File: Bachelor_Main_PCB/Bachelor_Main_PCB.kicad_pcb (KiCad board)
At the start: 4 copper layers, 200 x 81.5 mm, 220 parts, among them IC1 LD3985M18R, J1 M20-9990245, J11 F32Q-1A7H1-11022, J13 CONMHF1-SMD-G-T, J14 CONMHF1-SMD-G-T, J2 M20-9990245, J21 CONMHF1-SMD-G-T, J25 M20-9990245, J26 691137710002, J27 Conn_01x03_Pin, J28 691137710002, J29 M20-9990245, J4 MEM2075-00-140-01-A, J8 Conn_01x07_Pin, J9 M20-9990245, P1 SF70S006VBAR2000, Q1 SSM3J358R,LF, Q10 NX3008NBKW, Q11 SSM3J358R,LF, Q12 NX3008NBKW, Q13 BC817-40Q-13-F, Q2 SSM3J358R,LF, Q3 NX3008NBKW, Q4 NX3008NBKW, Q5 NX3008NBKW, Q6 NX3008NBKW, Q7 NX3008NBKW, Q8 NX3008NBKW, Q9 NX3008NBKW, U1 USB3320C-EZK-TR, U10 LMR51450FNDRRR, U11 USB2514B-I/M2, U2 STM32H7A3ZITxQ, U3 ESD7004MUTAG, U4 ESD7004MUTAG, U5 SC0683, U6 ESD7004MUTAG, U7 RC7620_1104627, U8 LM73100RPWR, U9 LMR51450FNDRRR, Y1 ECS-327TXO-30-TR, Y2 SG-210STF 24Mhz

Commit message: add gnd plane and fixed MCU bypass cap trace error
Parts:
- moved R18 93.2 mm to (153.2, 66.3), turned to 180 degrees
- moved R17 89.0 mm to (152.4, 68.8), turned to 90 degrees
- moved R16 85.8 mm to (148.3, 69.5)
- moved D4 85.3 mm to (152.4, 77.7), turned to 180 degrees
- moved Q2 84.0 mm to (148.4, 72.9), turned to -90 degrees
- moved J9 84.0 mm to (144.9, 68.7), turned to -90 degrees
- moved Q3 81.0 mm to (151.6, 72.7), turned to -90 degrees
- moved R19 80.4 mm to (149.2, 77.7)
- moved J11 77.8 mm to (94.6, 50.8), turned to 0 degrees
- moved J8 30.1 mm to (68.8, 105.3)
- moved Q6 1.46 mm to (209.9, 79.0)
- moved R29 1.46 mm to (209.7, 81.5)
- moved R30 1.46 mm to (209.7, 76.2)
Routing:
- net GND: track 54.3 -> 47.7 mm
- net +3V5_MCU: track 53.9 -> 48.8 mm
- added copper zone on In1.Cu, net GND

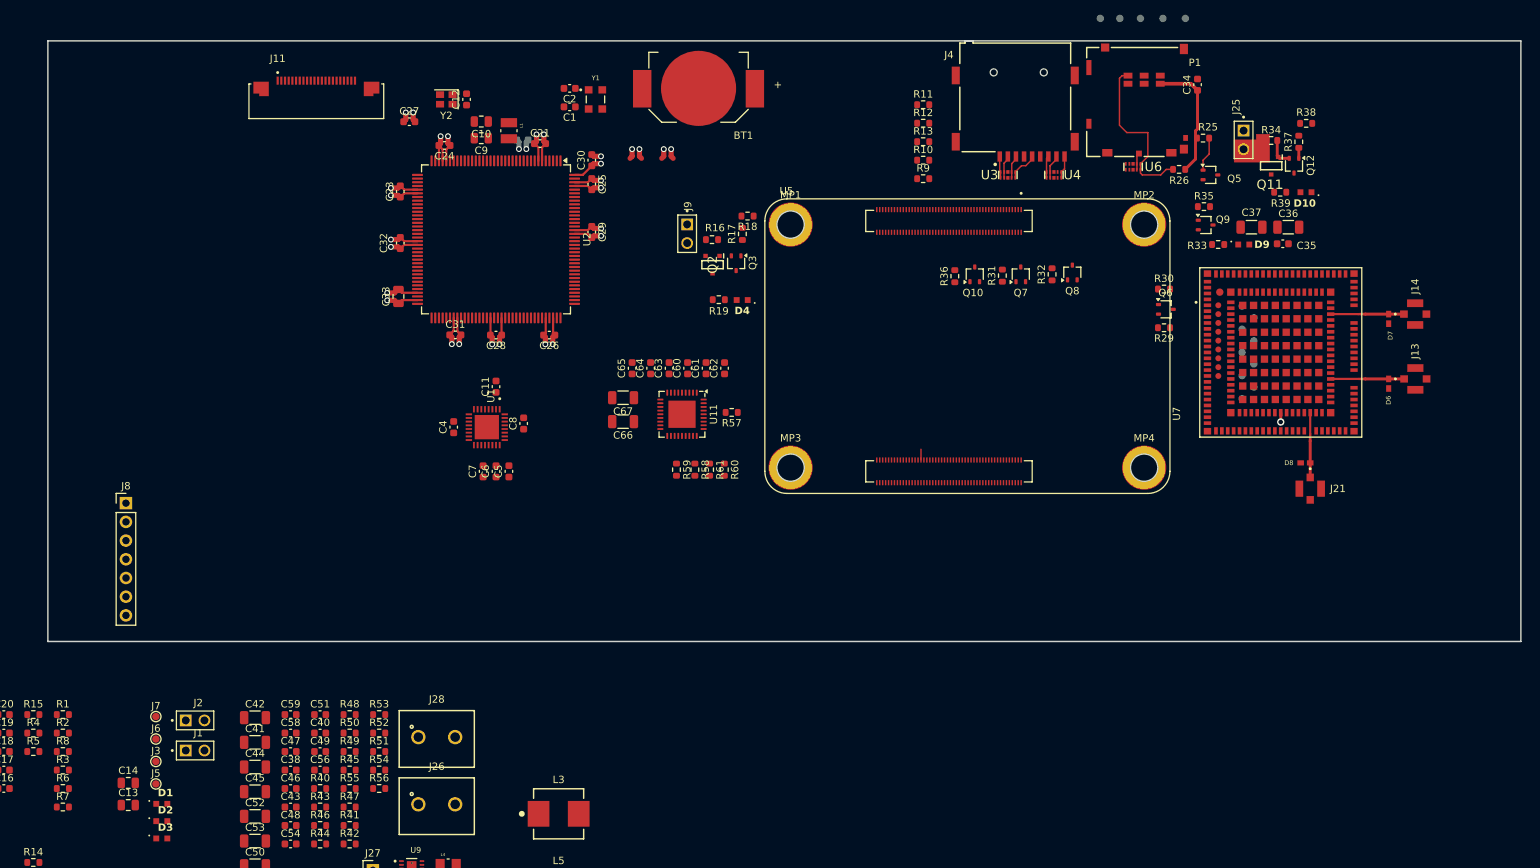
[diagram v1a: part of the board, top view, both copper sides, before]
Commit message: Updated gnd planes
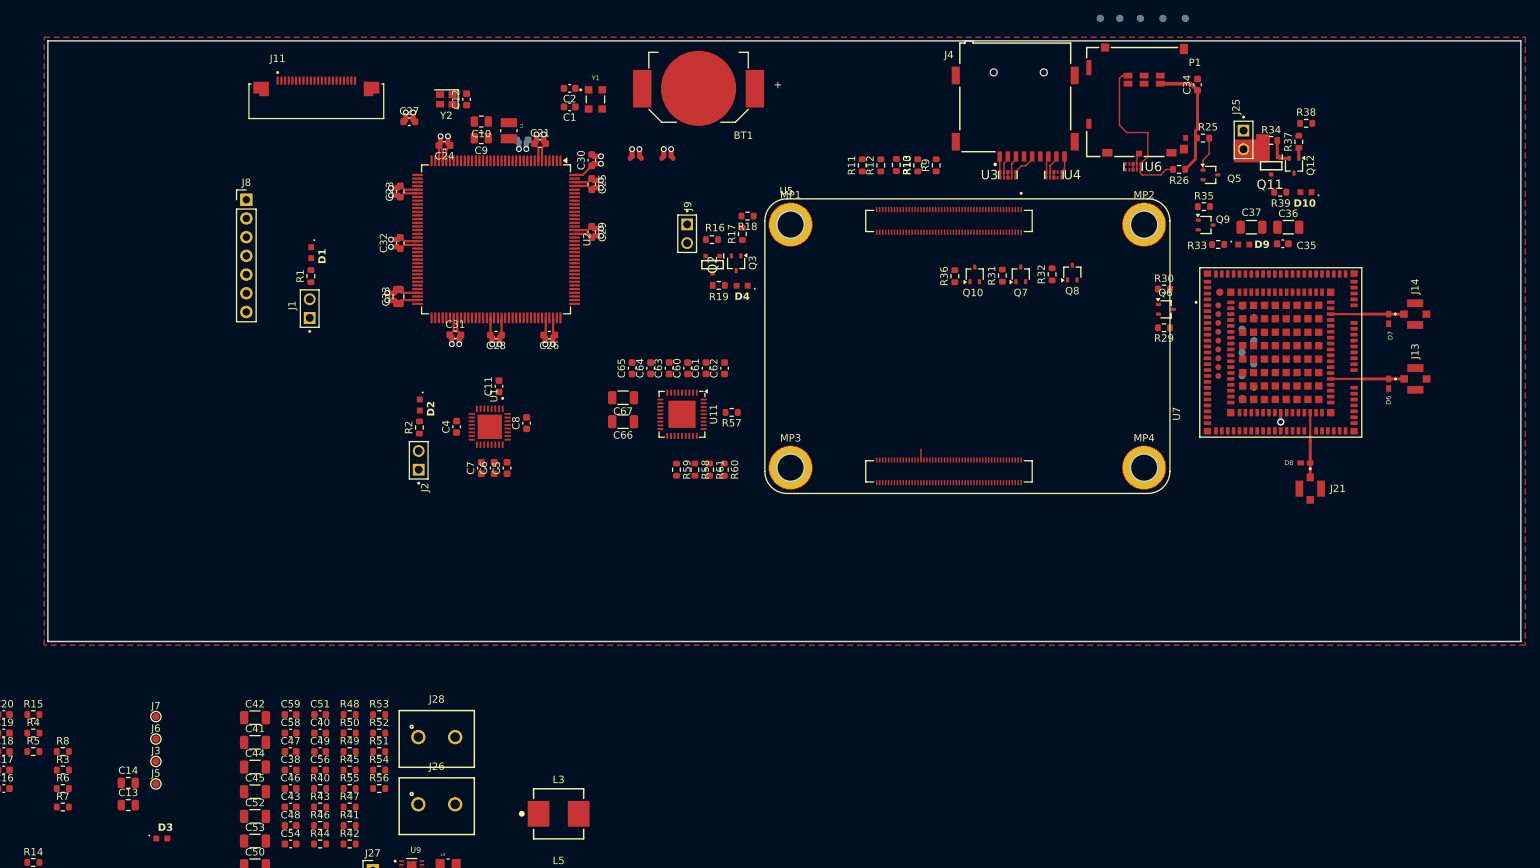
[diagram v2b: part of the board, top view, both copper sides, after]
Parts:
- moved D1 77.5 mm to (93.9, 71.3), turned to -90 degrees
- moved R1 68.4 mm to (93.9, 74.5), turned to 90 degrees
- moved D2 66.5 mm to (108.7, 92.0), turned to -90 degrees
- moved R2 63.8 mm to (108.6, 95.0), turned to 90 degrees
- moved J1 62.0 mm to (93.7, 78.9), turned to 90 degrees
- moved J2 46.6 mm to (108.5, 99.5), turned to 90 degrees
- moved J8 44.3 mm to (85.1, 64.1)
- moved R11 11.7 mm to (168.7, 59.5), turned to 90 degrees
- moved R12 8.12 mm to (171.2, 59.5), turned to 90 degrees
- moved R13 4.83 mm to (173.3, 59.4), turned to -90 degrees
- moved R9 2.53 mm to (178.8, 59.5), turned to 90 degrees
- moved D4 1.94 mm to (152.4, 75.8)
- moved R19 1.94 mm to (149.2, 75.8)
- moved R10 1.02 mm to (176.3, 59.5), turned to 90 degrees
- moved C5 0.51 mm to (120.5, 100.5)
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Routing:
- net GND: track 47.7 -> 50.1 mm
- added copper zone on F.Cu, net GND

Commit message: MODEM testppoints and gnd fill
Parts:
- T1, T2, T3, T4: moved to B.Cu
- moved T3 156.7 mm to (212.2, 79.5)
- moved T1 153.2 mm to (213.8, 81.0)
- moved T2 152.6 mm to (213.4, 84.8)
- moved T4 147.0 mm to (212.6, 82.8)
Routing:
- net Net-(U7A-J8): track 0.00 -> 7.43 mm, vias 0 -> 1
- net Net-(U7A-UART1_RTS): track 0.00 -> 7.36 mm, vias 0 -> 1
- net Net-(U7A-J6): track 0.00 -> 7.13 mm, vias 0 -> 1
- net Net-(U7A-J4): track 0.00 -> 6.82 mm, vias 0 -> 1
- net Net-(U7A-J2): track 0.00 -> 6.52 mm, vias 0 -> 1
- net Net-(U7A-UART1_TX): track 0.00 -> 6.37 mm, vias 0 -> 1
- net Net-(U7A-J9): track 0.00 -> 6.00 mm, vias 0 -> 1
- net Net-(U7A-J7): track 0.00 -> 5.69 mm, vias 0 -> 1
- net Net-(U7A-J5): track 0.00 -> 5.38 mm, vias 0 -> 1
- net Net-(U7A-J3): track 0.00 -> 5.32 mm, vias 0 -> 1
- net Net-(U7A-J1): track 0.00 -> 5.00 mm, vias 0 -> 1
- net GND: vias 15 -> 26

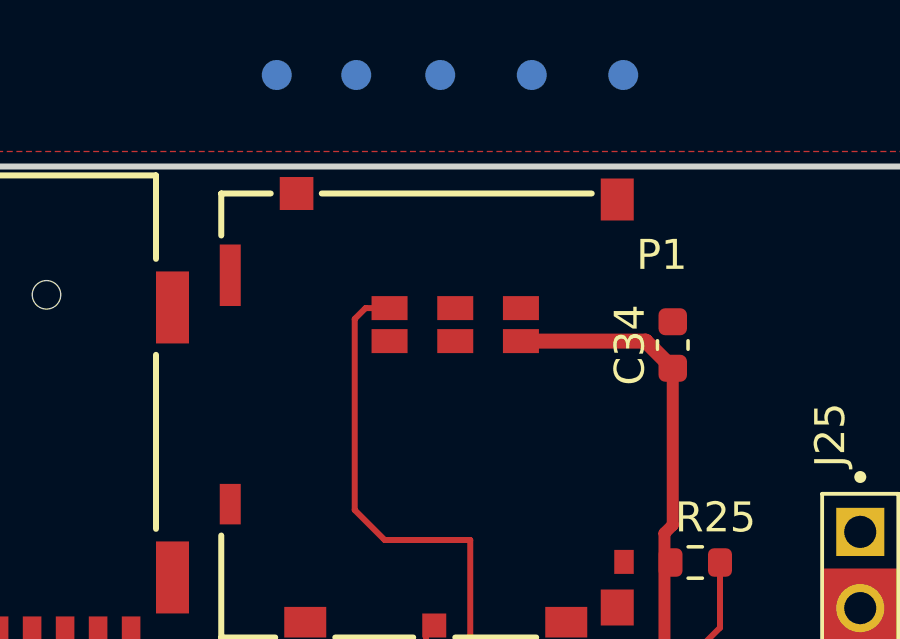
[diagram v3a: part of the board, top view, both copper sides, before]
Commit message: Sim card testpoints
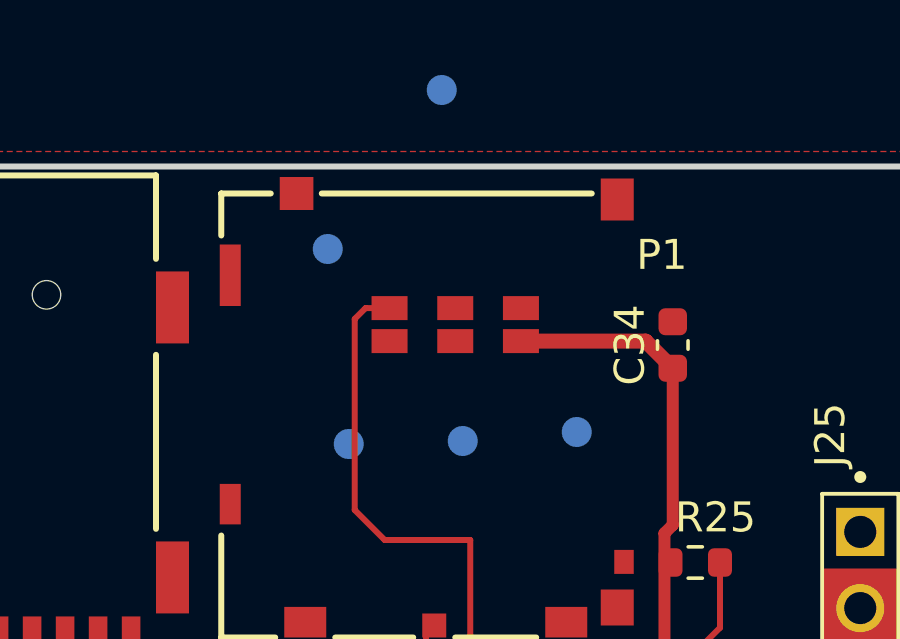
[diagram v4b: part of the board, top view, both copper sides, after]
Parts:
- moved T10 15.5 mm to (211.1, 51.4)
- moved T8 13.7 mm to (203.4, 51.8)
- moved T9 12.2 mm to (207.2, 51.7)
- moved T7 11.4 mm to (202.8, 45.3)
- moved T6 2.89 mm to (206.6, 40.0)
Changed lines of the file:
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@@
 	(footprint "TestPoint:TestPoint_Pad_D1.0mm"
 		(layer "B.Cu")
-		(at 206.5 39.5 90)
+		(at 207.25 51.7 90)
 		(descr "SMD pad as test Point, diameter 1.0mm")
 		(tags "test point SMD pad")
@@
 	(footprint "TestPoint:TestPoint_Pad_D1.0mm"
 		(layer "B.Cu")
-		(at 212.6 39.5 90)
+		(at 202.75 45.3 90)
 		(descr "SMD pad as test Point, diameter 1.0mm")
 		(tags "test point SMD pad")
@@
 	(footprint "TestPoint:TestPoint_Pad_D1.0mm"
 		(layer "B.Cu")
-		(at 203.7 39.5 90)
+		(at 206.55 40 90)
 		(descr "SMD pad as test Point, diameter 1.0mm")
 		(tags "test point SMD pad")
@@
 	(footprint "TestPoint:TestPoint_Pad_D1.0mm"
 		(layer "B.Cu")
-		(at 209.55 39.5 90)
+		(at 203.45 51.8 90)
 		(descr "SMD pad as test Point, diameter 1.0mm")
 		(tags "test point SMD pad")
@@
 	(footprint "TestPoint:TestPoint_Pad_D1.0mm"
 		(layer "B.Cu")
-		(at 201.05 39.5 90)
+		(at 211.05 51.4 90)
 		(descr "SMD pad as test Point, diameter 1.0mm")
 		(tags "test point SMD pad")

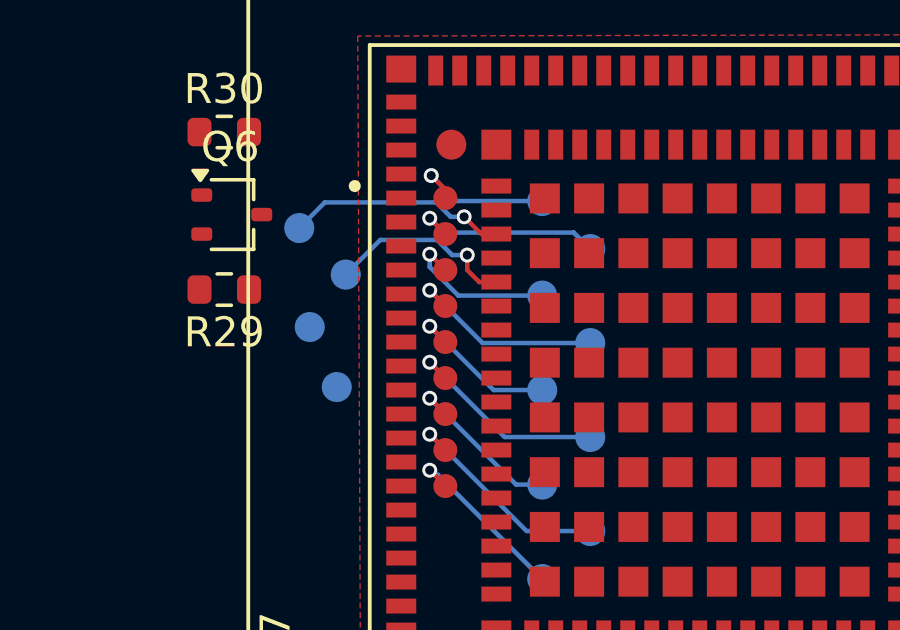
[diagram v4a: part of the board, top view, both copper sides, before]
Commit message: complete Modem testpoints
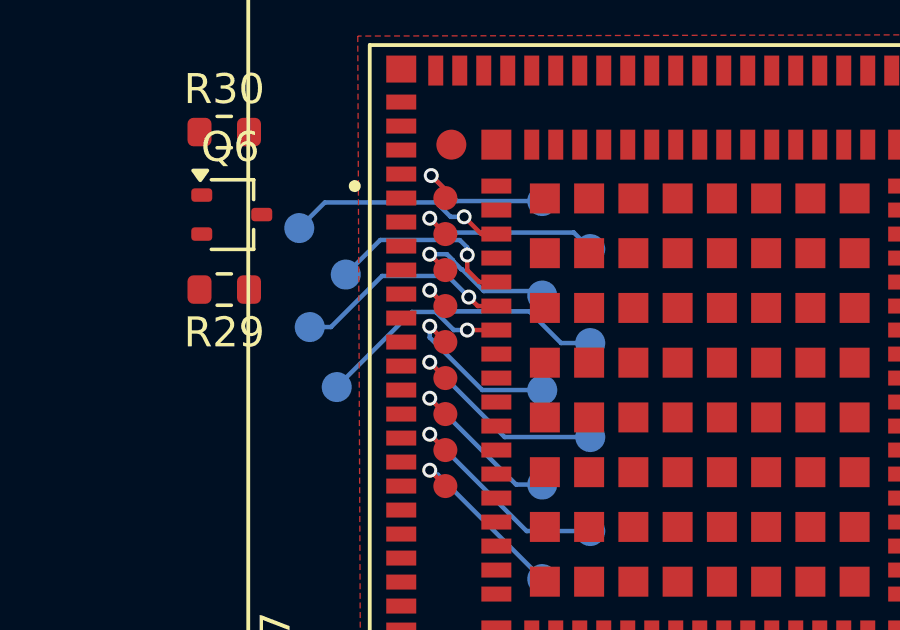
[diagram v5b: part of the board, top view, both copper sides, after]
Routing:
- net Net-(U7A-UART1_RX): track 0.00 -> 7.34 mm, vias 0 -> 1
- net Net-(U7A-UART1_DTR): track 0.00 -> 6.61 mm, vias 0 -> 1
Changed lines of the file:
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@@
 	)
 	(segment
-		(start 217.5 81.7)
+		(start 218.35 81.55)
+		(end 220.15 81.55)
+		(width 0.15)
+		(layer "B.Cu")
+		(net 126)
+	)
+	(segment
+		(start 217.626 80.826)
+		(end 218.35 81.55)
+		(width 0.15)
+		(layer "B.Cu")
+		(net 126)
+	)
+	(segment
+		(start 217.324 80.547166)
+		(end 217.602834 80.826)
+		(width 0.15)
+		(layer "B.Cu")
+		(net 126)
+	)
+	(segment
+		(start 217.121969 80.321969)
+		(end 217.324 80.524)
+		(width 0.15)
+		(layer "B.Cu")
+		(net 126)
+	)
+	(segment
+		(start 217.602834 80.826)
+		(end 217.626 80.826)
+		(width 0.15)
+		(layer "B.Cu")
+		(net 126)
+	)
+	(segment
+		(start 216.549465 80.321969)
+		(end 217.121969 80.321969)
+		(width 0.15)
+		(layer "B.Cu")
+		(net 126)
+	)
+	(segment
+		(start 220.15 81.55)
 		(end 220.3 81.7)
 		(width 0.15)
@@
 	)
 	(segment
-		(start 216.549465 80.749465)
-		(end 217.5 81.7)
-		(width 0.15)
-		(layer "B.Cu")
-		(net 126)
-	)
-	(segment
-		(start 216.549465 80.321969)
-		(end 216.549465 80.749465)
+		(start 217.324 80.524)
+		(end 217.324 80.547166)
 		(width 0.15)
 		(layer "B.Cu")
@@
 	)
 	(segment
-		(start 218.310949 83.283333)
+		(start 219.869991 82.226)
+		(end 220.927324 83.283333)
+		(width 0.15)
+		(layer "B.Cu")
+		(net 127)
+	)
+	(segment
+		(start 220.927324 83.283333)
 		(end 221.9 83.283333)
 		(width 0.15)
@@
 	(segment
 		(start 216.550002 81.522386)
-		(end 218.310949 83.283333)
+		(end 217.253616 82.226)
+		(width 0.15)
+		(layer "B.Cu")
+		(net 127)
+	)
+	(segment
+		(start 217.253616 82.226)
+		(end 219.869991 82.226)
 		(width 0.15)
 		(layer "B.Cu")
@@
 	)
 	(segment
-		(start 218.677495 84.85)
+		(start 218.3 84.85)
 		(end 220.3 84.85)
 		(width 0.15)
@@
 	)
 	(segment
+		(start 216.549465 83.099465)
+		(end 218.3 84.85)
+		(width 0.15)
+		(layer "B.Cu")
+		(net 128)
+	)
+	(segment
 		(start 216.549465 82.72197)
-		(end 218.677495 84.85)
+		(end 216.549465 83.099465)
 		(width 0.15)
 		(layer "B.Cu")
@@
 	)
 	(segment
-		(start 217.3 80.35)
-		(end 216.795969 79.845969)
+		(start 216.918617 79.845969)
+		(end 214.904031 79.845969)
+		(width 0.15)
+		(layer "B.Cu")
+		(net 153)
+	)
+	(segment
+		(start 217.8 80.35)
+		(end 217.8 80.1)
+		(width 0.15)
+		(layer "B.Cu")
+		(net 153)
+	)
+	(segment
+		(start 217.8 80.1)
+		(end 217.551 79.851)
+		(width 0.15)
+		(layer "B.Cu")
+		(net 153)
+	)
+	(segment
+		(start 216.923648 79.851)
+		(end 216.918617 79.845969)
 		(width 0.15)
 		(layer "B.Cu")
@@
 	)
 	(segment
-		(start 217.8 80.35)
-		(end 217.3 80.35)
-		(width 0.15)
-		(layer "B.Cu")
-		(net 153)
-	)
-	(segment
-		(start 216.795969 79.845969)
-		(end 214.904031 79.845969)
-		(width 0.15)
-		(layer "B.Cu")
-		(net 153)
+		(start 217.131584 79.851)
+		(end 216.923648 79.851)
+		(width 0.15)
+		(layer "B.Cu")
+		(net 153)
+	)
+	(segment
+		(start 217.551 79.851)
+		(end 217.131584 79.851)
+		(width 0.15)
+		(layer "B.Cu")
+		(net 153)
+	)
+	(segment
+		(start 217.8 82.85)
+		(end 218.77 82.85)
+		(width 0.15)
+		(layer "F.Cu")
+		(net 154)
+	)
+	(via
+		(at 217.8 82.85)
+		(size 0.5)
+		(drill 0.3)
+		(layers "F.Cu" "B.Cu")
+		(net 154)
+	)
+	(segment
+		(start 217.8 82.85)
+		(end 217.350661 82.85)
+		(width 0.15)
+		(layer "B.Cu")
+		(net 154)
+	)
+	(segment
+		(start 216.746631 82.24597)
+		(end 215.95403 82.24597)
+		(width 0.15)
+		(layer "B.Cu")
+		(net 154)
+	)
+	(segment
+		(start 217.350661 82.85)
+		(end 216.746631 82.24597)
+		(width 0.15)
+		(layer "B.Cu")
+		(net 154)
+	)
+	(segment
+		(start 215.95403 82.24597)
+		(end 213.45 84.75)
+		(width 0.15)
+		(layer "B.Cu")
+		(net 154)
 	)
 	(segment
@@
 		(layer "B.Cu")
 		(net 155)
+	)
+	(segment
+		(start 218.15 82.05)
+		(end 218.77 82.05)
+		(width 0.15)
+		(layer "F.Cu")
+		(net 156)
+	)
+	(segment
+		(start 217.85 81.75)
+		(end 218.15 82.05)
+		(width 0.15)
+		(layer "F.Cu")
+		(net 156)
+	)
+	(via
+		(at 217.85 81.75)
+		(size 0.5)
+		(drill 0.3)
+		(layers "F.Cu" "B.Cu")
+		(net 156)
+	)
+	(segment
+		(start 214.96072 81.046386)
+		(end 213.257106 82.75)
+		(width 0.15)
+		(layer "B.Cu")
+		(net 156)
+	)
+	(segment
+		(start 217.85 81.75)
+		(end 217.146386 81.046386)
+		(width 0.15)
+		(layer "B.Cu")
+		(net 156)
+	)
+	(segment
+		(start 213.257106 82.75)
+		(end 212.55 82.75)
+		(width 0.15)
+		(layer "B.Cu")
+		(net 156)
+	)
+	(segment
+		(start 217.146386 81.046386)
+		(end 214.96072 81.046386)
+		(width 0.15)
+		(layer "B.Cu")
+		(net 156)
 	)
 	(segment
@@
 			(pts
 				(xy 57.65 42.05) (xy 258.75 42.05) (xy 258.75 124.6) (xy 57.65 124.6)
+			)
+		)
+	)
+	(zone
+		(net 7)
+		(net_name "/Wireless modem/UIM_VCC")
+		(layer "F.Cu")
+		(name "$teardrop_padvia$")
+		(hatch full 0.1)
+		(priority 30000)
+		(attr
+			(teardrop
+				(type padvia)
+			)
+		)
+		(connect_pads yes
+			(clearance 0)
+		)
+		(min_thickness 0.0254)
+		(filled_areas_thickness no)
+		(fill yes
+			(thermal_gap 0.5)
+			(thermal_bridge_width 0.5)
+			(island_removal_mode 1)
+			(island_area_min 10)
+		)
+		(polygon
+			(pts
+				(xy 225.75 93.309605) (xy 225.35 93.309605) (xy 225.059607 94.202453) (xy 225.55 94.300998) (xy 226.040393 94.202453)
 			)
 		)
@@
 			)
 		)
-	)
-	(zone
-		(net 7)
-		(net_name "/Wireless modem/UIM_VCC")
-		(layer "F.Cu")
-		(name "$teardrop_padvia$")
-		(hatch full 0.1)
-		(priority 30000)
-		(attr
-			(teardrop
-				(type padvia)
-			)
-		)
-		(connect_pads yes
-			(clearance 0)
-		)
-		(min_thickness 0.0254)
-		(filled_areas_thickness no)
-		(fill yes
-			(thermal_gap 0.5)
-			(thermal_bridge_width 0.5)
-			(island_removal_mode 1)
-			(island_area_min 10)
-		)
-		(polygon
-			(pts
-				(xy 225.75 93.309605) (xy 225.35 93.309605) (xy 225.059607 94.202453) (xy 225.55 94.300998) (xy 226.040393 94.202453)
-			)
-		)
